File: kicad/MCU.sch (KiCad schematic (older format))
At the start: 37 parts, among them J10 Conn_01x04, J11 TC2050-IDC, J7 DAC1_OUT1, J8 ADC1_IN1, J9 GPIO_OUT PB15, Q1 SI2374DS-T1-GE3, Q2 SI2374DS-T1-GE3, SW1 SW_Push, U1 STM32F303VETx, Y1 NX3225GD-8MHZ-EXS00A-CG04874

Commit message: Power supply layout
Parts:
- renumbered C9 to C11, C10 to C12, C11 to C13, C12 to C14, C13 to C15, C14 to C16, C15 to C17, C16 to C18, C17 to C19, C18 to C20, C19 to C21, C20 to C22, C21 to C23, C22 to C24, C23 to C25, C24 to C26, C25 to C27, C26 to C28, J9 to J10, J10 to J11, J11 to J12, J7 to J8, J8 to J9

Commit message: Start MCU layout
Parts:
- removed J11: Conn_01x04, Connector_PinHeader_2.54mm:PinHeader_1x04_P2.54mm_Vertical, symbol Connector_Generic:Conn_01x04
- added J11: S4B-PH-KL_LF__SN_, SamacSys_Parts:S4BPHKLLFSN, symbol SamacSys_Parts:S4B-PH-KL_LF__SN_
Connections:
- net GND: now also J11.4
- net VDD: now also J11.3
- net at U1.93 (PB7): now also J11.1
- net at U1.92 (PB6): now also J11.2
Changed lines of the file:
@@
 NoConn ~ 9400 4150
 NoConn ~ 9100 4150
-$Comp
-L Connector_Generic:Conn_01x04 J11
-U 1 1 604DEBF3
-P 6800 5200
-F 0 "J11" H 6718 4775 50  0000 C CNN
-F 1 "Conn_01x04" H 6718 4866 50  0000 C CNN
-F 2 "Connector_PinHeader_2.54mm:PinHeader_1x04_P2.54mm_Vertical" H 6800 5200 50  0001 C CNN
-F 3 "~" H 6800 5200 50  0001 C CNN
-	1    6800 5200
-	1    0    0    1
-$EndComp
 Wire Wire Line
 	6050 5300 6600 5300
-Wire Wire Line
-	6050 5200 6150 5200
-Wire Wire Line
-	6150 5200 6150 5100
-Wire Wire Line
-	6150 5100 6600 5100
-$Comp
-L power:GND #PWR042
+$Comp
+L power:GND #PWR044
 U 1 1 604FA647
-P 6550 5200
-F 0 "#PWR042" H 6550 4950 50  0001 C CNN
-F 1 "GND" V 6555 5072 50  0000 R CNN
-F 2 "" H 6550 5200 50  0001 C CNN
-F 3 "" H 6550 5200 50  0001 C CNN
-	1    6550 5200
+P 6600 5000
+F 0 "#PWR044" H 6600 4750 50  0001 C CNN
+F 1 "GND" V 6500 5050 50  0000 R CNN
+F 2 "" H 6600 5000 50  0001 C CNN
+F 3 "" H 6600 5000 50  0001 C CNN
+	1    6600 5000
 	0    1    1    0
 $EndComp
-Wire Wire Line
-	6550 5200 6600 5200
 $Comp
 L power:VDD #PWR039
 U 1 1 604FF675
-P 6350 5000
-F 0 "#PWR039" H 6350 4850 50  0001 C CNN
-F 1 "VDD" H 6365 5173 50  0000 C CNN
-F 2 "" H 6350 5000 50  0001 C CNN
-F 3 "" H 6350 5000 50  0001 C CNN
-	1    6350 5000
-	1    0    0    -1
-$EndComp
-Wire Wire Line
-	6350 5000 6600 5000
+P 6350 5100
+F 0 "#PWR039" H 6350 4950 50  0001 C CNN
+F 1 "VDD" H 6365 5273 50  0000 C CNN
+F 2 "" H 6350 5100 50  0001 C CNN
+F 3 "" H 6350 5100 50  0001 C CNN
+	1    6350 5100
+	1    0    0    -1
+$EndComp
+Wire Wire Line
+	6350 5100 6600 5100
 $Comp
 L power:GND #PWR045
@@
 Connection ~ 6100 5000
 $Comp
-L power:GND #PWR043
+L power:GND #PWR042
 U 1 1 6074645D
 P 6550 5700
-F 0 "#PWR043" H 6550 5450 50  0001 C CNN
+F 0 "#PWR042" H 6550 5450 50  0001 C CNN
 F 1 "GND" H 6555 5527 50  0000 C CNN
 F 2 "" H 6550 5700 50  0001 C CNN
@@
 	6400 5900 6400 5800
 $Comp
-L power:GND #PWR044
+L power:GND #PWR043
 U 1 1 607C1FDF
 P 6550 6650
-F 0 "#PWR044" H 6550 6400 50  0001 C CNN
+F 0 "#PWR043" H 6550 6400 50  0001 C CNN
 F 1 "GND" H 6555 6477 50  0000 C CNN
 F 2 "" H 6550 6650 50  0001 C CNN
@@
 Wire Wire Line
 	5050 2500 5050 2600
+$Comp
+L SamacSys_Parts:S4B-PH-KL_LF__SN_ J11
+U 1 1 6067E8E3
+P 6600 5000
+F 0 "J11" H 7228 4896 50  0000 L CNN
+F 1 "S4B-PH-KL_LF__SN_" H 6650 4550 50  0000 L CNN
+F 2 "SamacSys_Parts:S4BPHKLLFSN" H 7250 5100 50  0001 L CNN
+F 3 "https://datasheet.lcsc.com/szlcsc/JST-Sales-America-S4B-PH-KL-LF-SN_C160235.pdf" H 7250 5000 50  0001 L CNN
+F 4 "CONN HEADER R/A 4POS 2MM" H 7250 4900 50  0001 L CNN "Description"
+F 5 "4.8" H 7250 4800 50  0001 L CNN "Height"
+F 6 "JST Sales America" H 7250 4700 50  0001 L CNN "Manufacturer_Name"
+F 7 "S4B-PH-KL(LF)(SN)" H 7250 4600 50  0001 L CNN "Manufacturer_Part_Number"
+F 8 "" H 7250 4500 50  0001 L CNN "Mouser Part Number"
+F 9 "" H 7250 4400 50  0001 L CNN "Mouser Price/Stock"
+F 10 "" H 7250 4300 50  0001 L CNN "Arrow Part Number"
+F 11 "" H 7250 4200 50  0001 L CNN "Arrow Price/Stock"
+	1    6600 5000
+	1    0    0    -1
+$EndComp
+Wire Wire Line
+	6050 5200 6600 5200
 $EndSCHEMATC

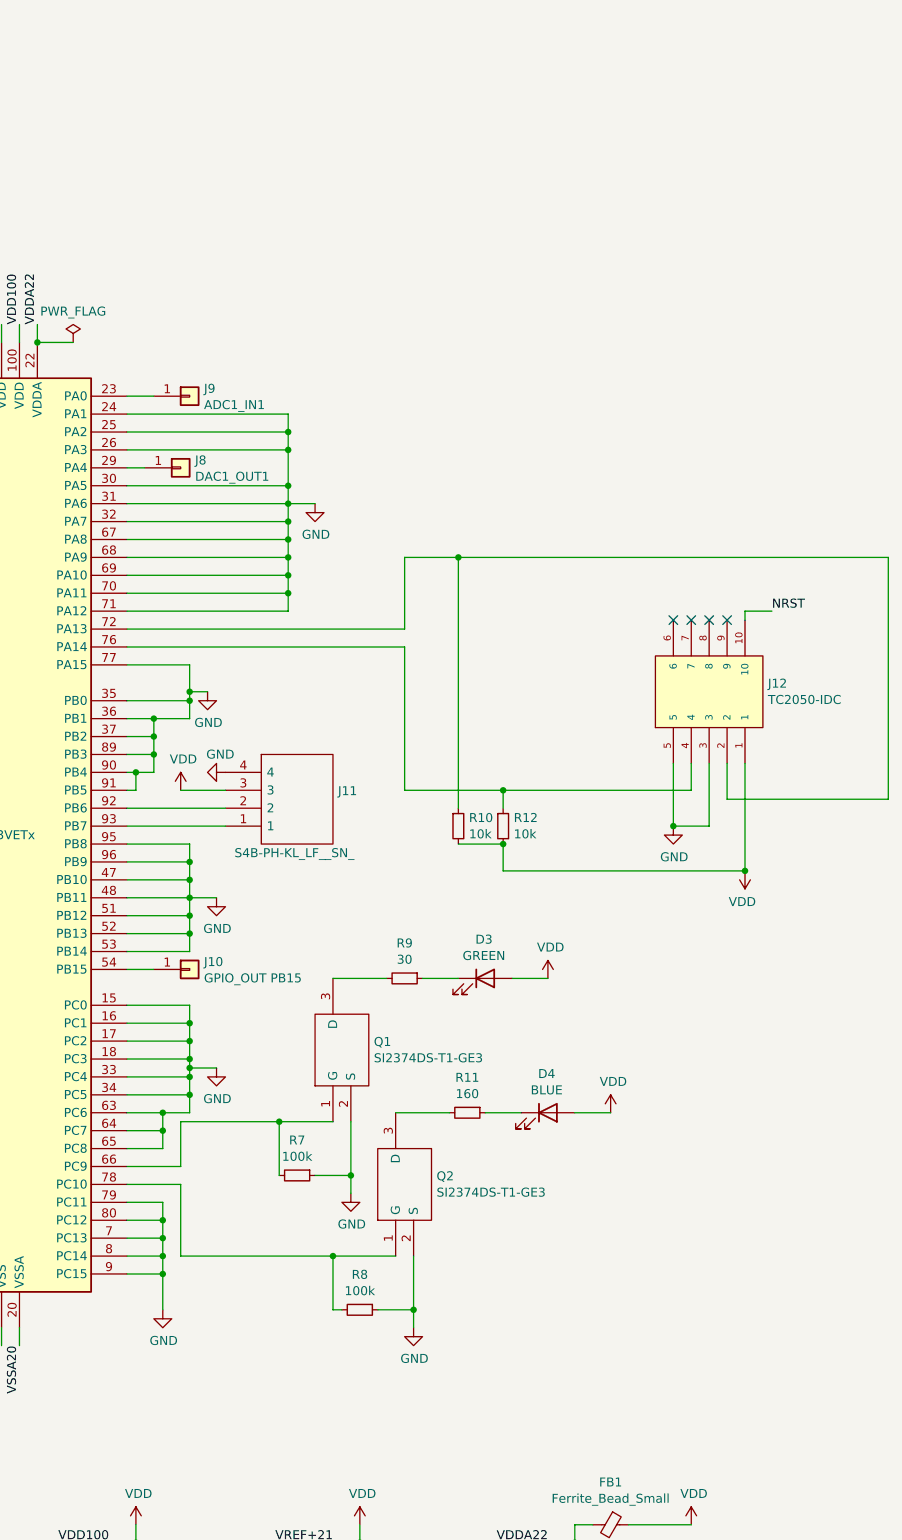
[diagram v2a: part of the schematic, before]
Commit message: Add USB
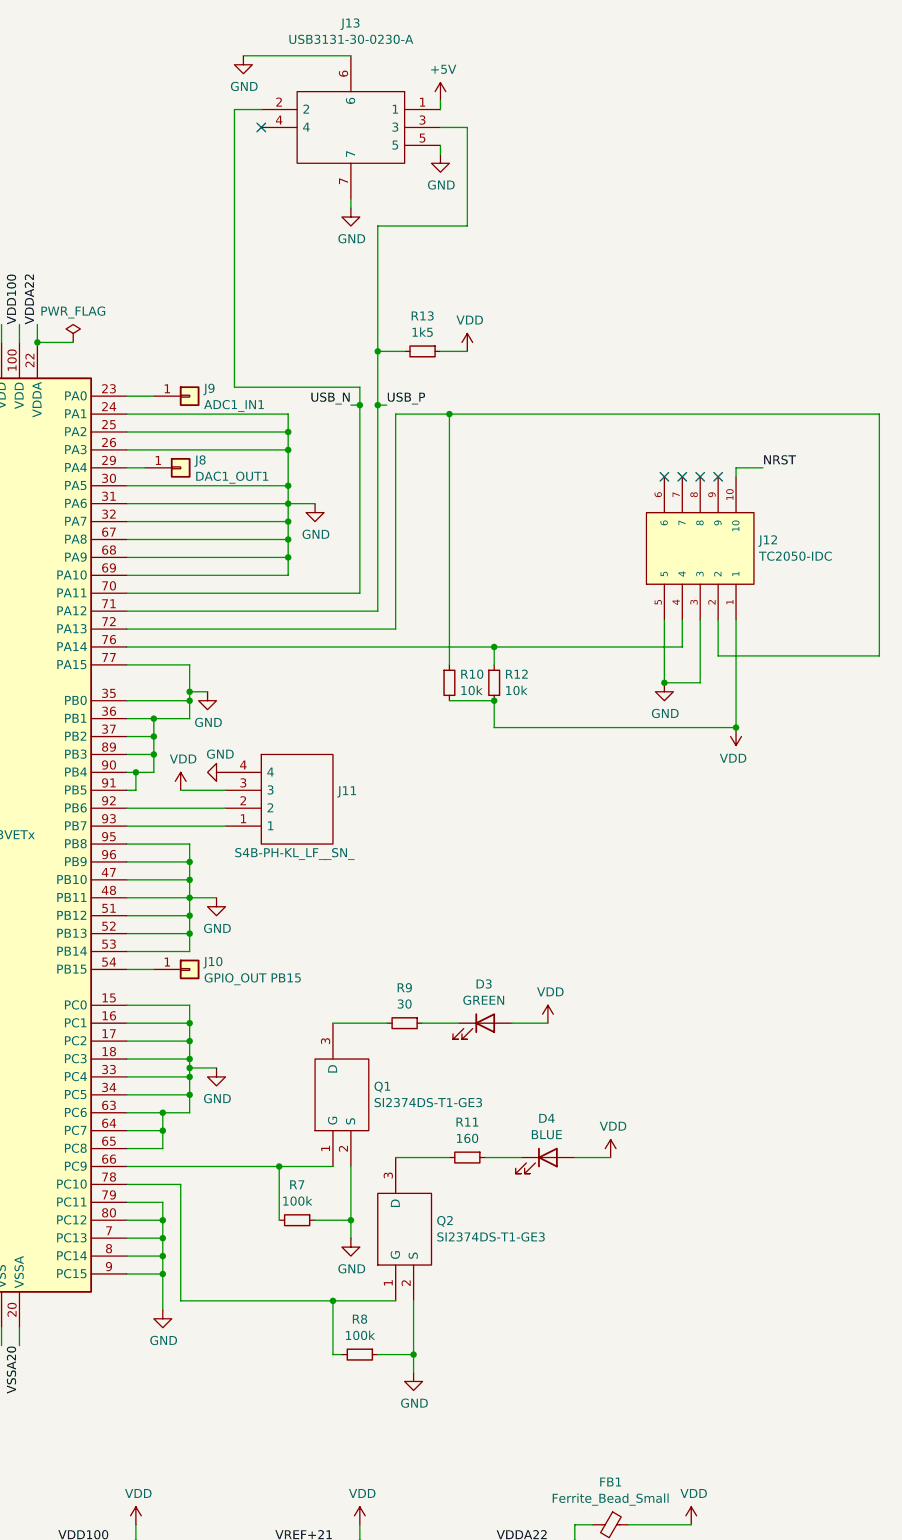
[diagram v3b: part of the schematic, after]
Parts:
- added J13: USB3131-30-0230-A, SamacSys_Parts:USB3131300230A, symbol SamacSys_Parts:USB3131-30-0230-A
- added R13: 1k5, Resistor_SMD:R_0603_1608Metric, symbol Device:R_Small
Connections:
- net GND: now also J13.5, J13.6, J13.7; no longer U1.70 (PA11), U1.71 (PA12)
- net VDD: now also R13.1
- new net +5V: J13.1
- new net USB_N: J13.2, U1.70 (PA11)
- new net USB_P: J13.3, R13.2, U1.71 (PA12)
- no-connect marks 4 -> 5
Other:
- moved on the sheet: D3, D4, J12, Q1, Q2, R10, R11, R12, R7, R8, R9

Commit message: Move docs to central collection; fine-tune schematic
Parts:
- removed U1: STM32F303VETx, Package_QFP:LQFP-100_14x14mm_P0.5mm, symbol MCU_ST_STM32F3:STM32F303VETx
- added IC?: STM32H757BIT6, QFP50P3000X3000X160-208N, symbol SamacSys_Parts:STM32H757BIT6
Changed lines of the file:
@@
 encoding utf-8
 Sheet 3 3
-Title "BasicSTM32"
-Date "2021-03-11"
-Rev "0.9.1"
+Title "BasicSTM32H757BI"
+Date "2021-07-19"
+Rev "0.9.0"
 Comp "Goozbazi LLC"
-Comment1 "Basic STM32F3 board for testing and development"
+Comment1 "Basic STM32H7 board template"
 Comment2 ""
 Comment3 ""
@@
 Wire Wire Line
 	5750 2600 5550 2600
-Connection ~ 5550 2600
 Wire Wire Line
 	5550 2600 5550 2500
@@
 Wire Wire Line
 	6350 7300 6350 7950
-$Comp
-L MCU_ST_STM32F3:STM32F303VETx U1
-U 1 1 6059FAAF
-P 5250 5300
-F 0 "U1" H 5250 5400 50  0000 C CNN
-F 1 "STM32F303VETx" H 5250 5250 50  0000 C CNN
-F 2 "Package_QFP:LQFP-100_14x14mm_P0.5mm" H 4650 2700 50  0001 R CNN
-F 3 "http://www.st.com/st-web-ui/static/active/en/resource/technical/document/datasheet/DM00118585.pdf" H 5250 5300 50  0001 C CNN
-	1    5250 5300
-	1    0    0    -1
-$EndComp
 $Comp
 L Connector_Generic:Conn_01x01 J8
@@
 Wire Wire Line
 	7300 1800 7300 1850
+$Comp
+L SamacSys_Parts:STM32H757BIT6 IC?
+U 1 1 60F919DF
+P 2900 11850
+F 0 "IC?" H 8644 9346 50  0000 L CNN
+F 1 "STM32H757BIT6" H 8644 9255 50  0000 L CNN
+F 2 "QFP50P3000X3000X160-208N" H 8450 12450 50  0001 L CNN
+F 3 "https://www.st.com/resource/en/datasheet/stm32h757ai.pdf" H 8450 12350 50  0001 L CNN
+F 4 "MCU 32-bit ARM Cortex M7/M4 RISC 2MB Flash 3.3V 208-Pin LQFP Tray" H 8450 12250 50  0001 L CNN "Description"
+F 5 "1.6" H 8450 12150 50  0001 L CNN "Height"
+F 6 "STMicroelectronics" H 8450 12050 50  0001 L CNN "Manufacturer_Name"
+F 7 "STM32H757BIT6" H 8450 11950 50  0001 L CNN "Manufacturer_Part_Number"
+F 8 "511-STM32H757BIT6" H 8450 11850 50  0001 L CNN "Mouser Part Number"
+F 9 "https://www.mouser.co.uk/ProductDetail/STMicroelectronics/STM32H757BIT6?qs=vLWxofP3U2y44i97M%252BIKWw%3D%3D" H 8450 11750 50  0001 L CNN "Mouser Price/Stock"
+F 10 "STM32H757BIT6" H 8450 11650 50  0001 L CNN "Arrow Part Number"
+F 11 "https://www.arrow.com/en/products/stm32h757bit6/stmicroelectronics?region=nac" H 8450 11550 50  0001 L CNN "Arrow Price/Stock"
+	1    2900 11850
+	1    0    0    -1
+$EndComp
 $EndSCHEMATC

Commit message: Place basic power; place osc, boot, nrst
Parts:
- added C? (x12): 100n, Capacitor_SMD:C_0603_1608Metric, symbol Device:C_Small
- added C? (x12): 1u, Capacitor_SMD:C_0603_1608Metric, symbol Device:C_Small
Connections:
- net labels added: VBAT08, VDD07, VDD108, VDD114, VDD117, VDD133, VDD155, VDD161, VDD17, VDD179, VDD187, VDD29, VDD49, VDD56, VDD74, VDD80, VDDA208, VREF+43, VSS06, VSS109, VSS113, VSS118, VSS132, VSS139, VSS153, VSS16, VSS160, VSS178, VSS186, VSS200, VSS207, VSS28, VSS50, VSS55, VSS73, VSS79, VSS90, VSSA207
- net labels removed: VBAT06, VDD28, VDD50, VDD75, VDDA22, VREF+21, VSS27, VSS49, VSS74, VSSA20
- wire segments 297 -> 394
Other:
- moved on the sheet: C11, C12, C13, C14, C15, C16, C17, C18, C19, C20, C21, C22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

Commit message: Complete power and ground
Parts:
- removed C13, C19, C20, C22, C24, C? (x12): 1u, Capacitor_SMD:C_0603_1608Metric, symbol Device:C_Small
- added C? (x6): 2.2u, Capacitor_SMD:C_0603_1608Metric, symbol Device:C_Small
- added C? (x3): 4.7u, Capacitor_SMD:C_0603_1608Metric, symbol Device:C_Small
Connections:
- net labels added: VCAP152, VCAP199, VCAP89, VDDA44, VDDLDO154, VDDLDO202, VDDLDO91, VSSA42
- net labels removed: VSSA207
- wire segments 394 -> 386
- no-connect marks 5 -> 6
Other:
- moved on the sheet: C12, C14, C27, C28, FB1, SW1
